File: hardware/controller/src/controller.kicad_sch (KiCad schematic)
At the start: 39 parts, among them J1 To Display, J2 Display, J3 Barrel_Jack_Switch, J4 Program, J5 JTAG, SW1 RESET, SW2 BTN1, SW3 BTN1, U1 ESP32-WROOM-E, U2 XL1509-5.0, U3 XL1509-3.3, U4 RS0102YH8

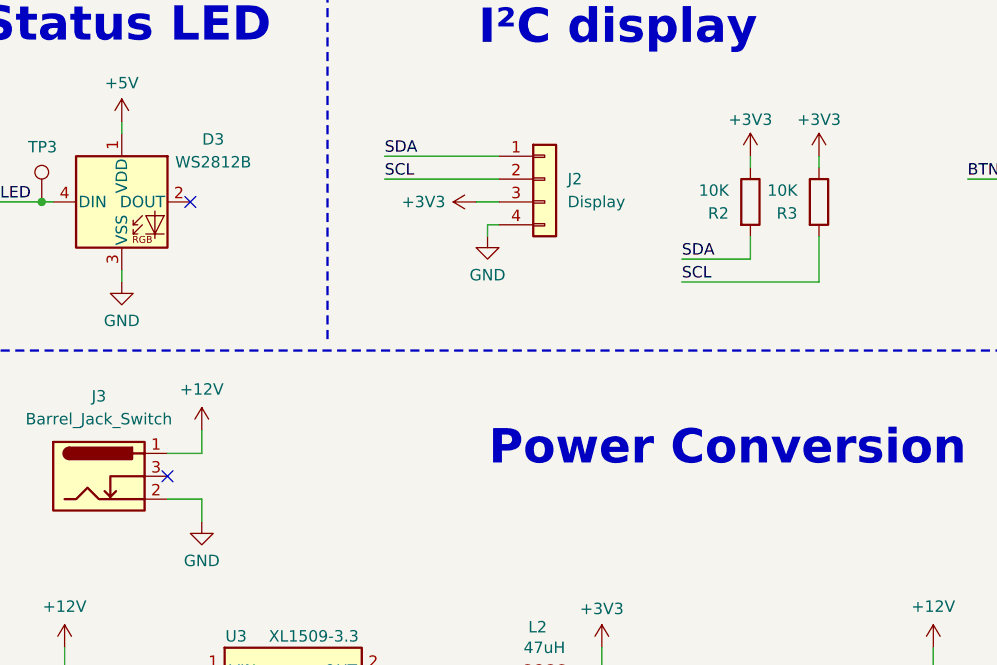
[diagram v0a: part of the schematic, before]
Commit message: connect dc jack ground pin
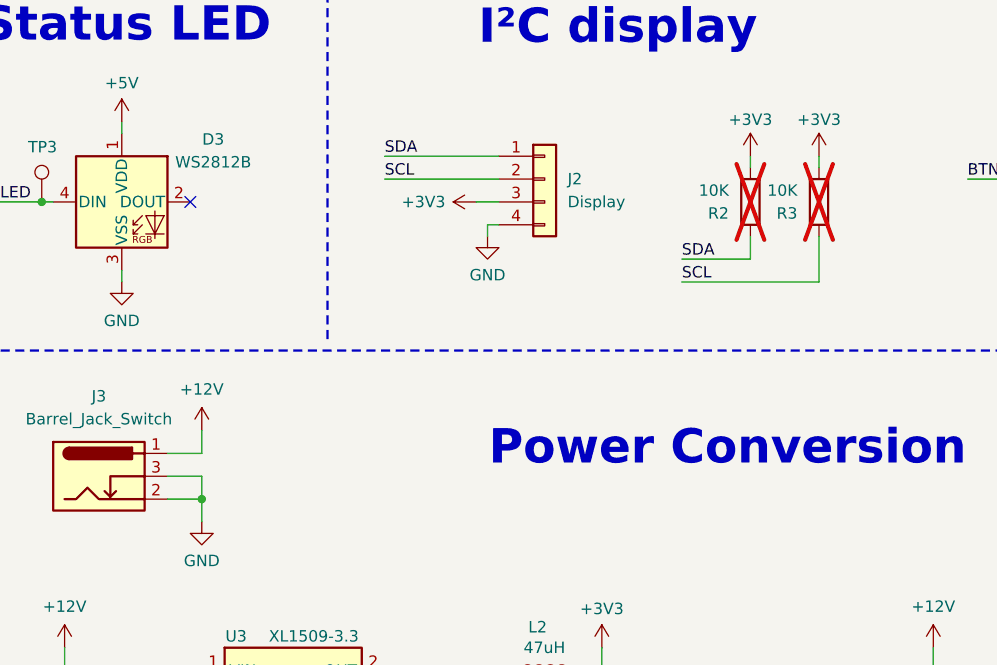
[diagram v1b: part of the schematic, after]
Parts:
- R2, R3: now not fitted; now left out of the parts list
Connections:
- net GND: now also J3.3
- no-connect marks 16 -> 15
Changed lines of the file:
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@@
 		(title "Controller")
 		(date "${DATE}")
-		(rev "2.0.3 DEV")
+		(rev "2.0.4 DEV")
 		(company "OpenFlap")
 		(comment 1 "${GIT_TAG}")
@@
 	)
 	(junction
+		(at 43.18 161.29)
+		(diameter 0)
+		(color 0 0 0 0)
+	)
+	(junction
 		(at 184.15 180.34)
 		(diameter 0)
@@
 	)
 	(no_connect
-		(at 39.37 158.75)
-	)
-	(no_connect
 		(at 100.33 68.58)
 	)
@@
 	(wire
 		(pts
+			(xy 43.18 158.75) (xy 43.18 161.29)
+		)
+		(stroke
+			(width 0)
+			(type default)
+		)
+	)
+	(wire
+		(pts
 			(xy 74.93 180.34) (xy 74.93 181.61)
 		)
@@
 	(wire
 		(pts
+			(xy 39.37 158.75) (xy 43.18 158.75)
+		)
+		(stroke
+			(width 0)
+			(type default)
+		)
+	)
+	(wire
+		(pts
 			(xy 128.27 125.73) (xy 134.62 125.73)
 		)
@@
 		(unit 1)
 		(exclude_from_sim no)
-		(in_bom yes)
+		(in_bom no)
 		(on_board yes)
-		(dnp no)
+		(dnp yes)
 		(property "Reference" "R3"
 			(at 108.204 129.54 0)
@@
 		(unit 1)
 		(exclude_from_sim no)
-		(in_bom yes)
+		(in_bom no)
 		(on_board yes)
-		(dnp no)
+		(dnp yes)
 		(property "Reference" "R2"
 			(at 100.584 129.54 0)

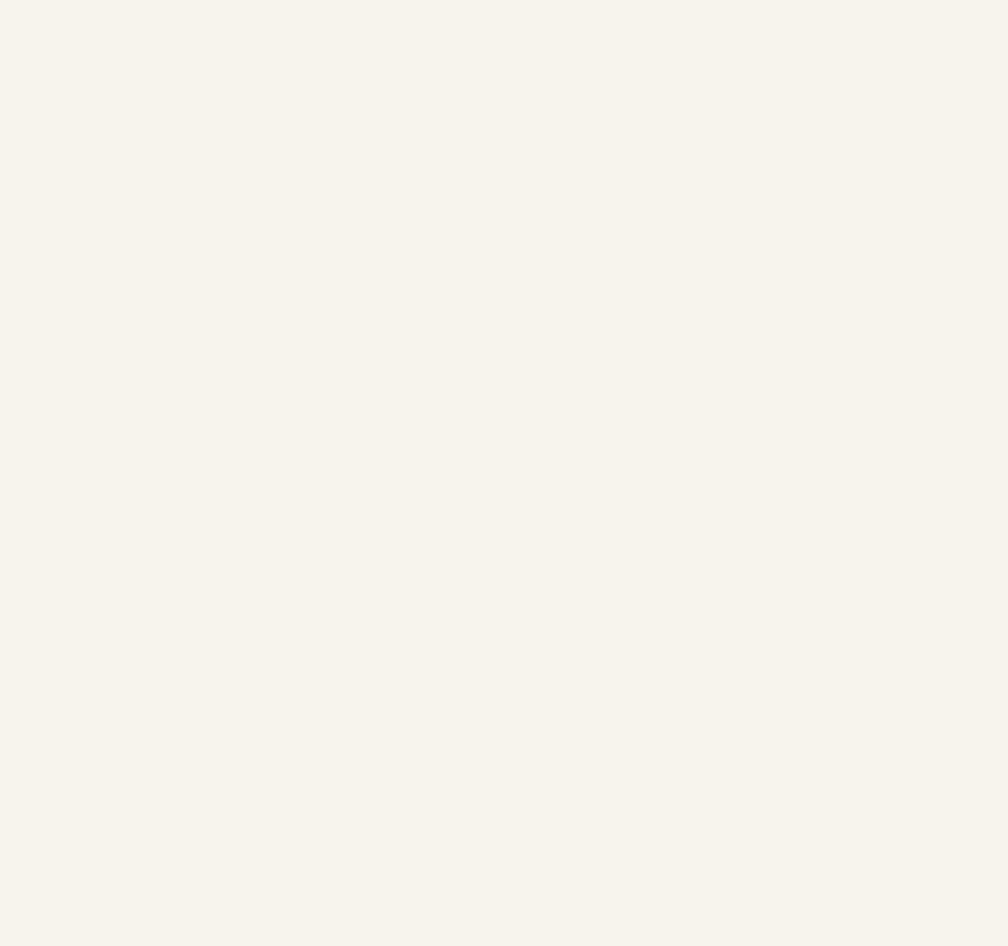
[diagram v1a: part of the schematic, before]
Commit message: Update side panel to add proper ESD protection, 12V detection, removed uart switch in favor of software switching, shuffled around some IO for improved routing.
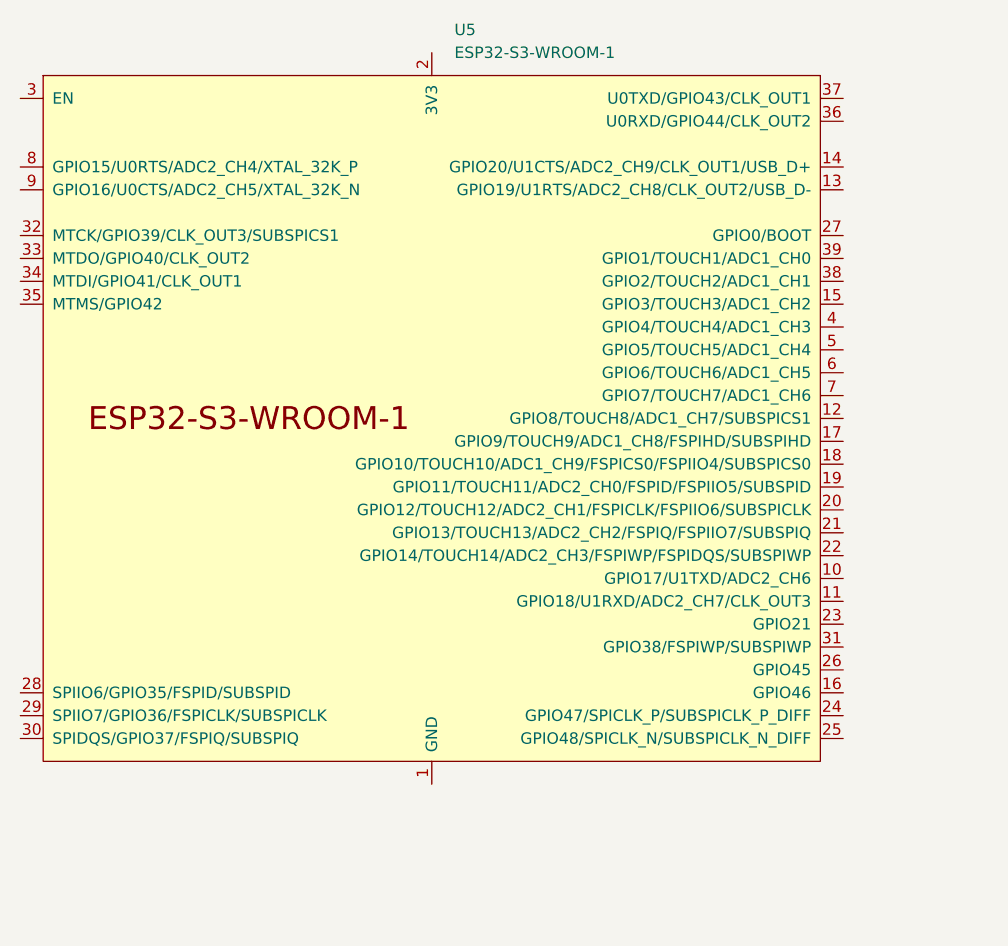
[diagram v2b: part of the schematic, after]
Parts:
- added U5: ESP32-S3-WROOM-1, PCM_Espressif:ESP32-S3-WROOM-1, symbol PCM_Espressif:ESP32-S3-WROOM-1
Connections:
- new net: U5.1 (GND), U5.40 (GND), U5.41 (GND)
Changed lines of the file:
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@@
+	)
+	(symbol
+		(lib_id "PCM_Espressif:ESP32-S3-WROOM-1")
+		(at -91.44 46.99 0)
+		(unit 1)
+		(exclude_from_sim no)
+		(in_bom yes)
+		(on_board yes)
+		(dnp no)
+		(fields_autoplaced yes)
+		(property "Reference" "U5"
+			(at -88.928 3.81 0)
+			(effects
+				(font
+					(size 1.27 1.27)
+				)
+				(justify left)
+			)
+		)
+		(property "Value" "ESP32-S3-WROOM-1"
+			(at -88.928 6.35 0)
+			(effects
+				(font
+					(size 1.27 1.27)
+				)
+				(justify left)
+			)
+		)
+		(property "Footprint" "PCM_Espressif:ESP32-S3-WROOM-1"
+			(at -88.9 95.25 0)
+			(effects
+				(font
+					(size 1.27 1.27)
+				)
+				(hide yes)
+			)
+		)
+		(property "Datasheet" "https://www.espressif.com/sites/default/files/documentation/esp32-s3-wroom-1_wroom-1u_datasheet_en.pdf"
+			(at -88.9 97.79 0)
+			(effects
+				(font
+					(size 1.27 1.27)
+				)
+				(hide yes)
+			)
+		)
+		(property "Description" "2.4 GHz WiFi (802.11 b/g/n) and Bluetooth ® 5 (LE) module Built around ESP32S3 series of SoCs, Xtensa ® dualcore 32bit LX7 microprocessor Flash up to 16 MB, PSRAM up to 8 MB 36 GPIOs, rich set of peripherals Onboard PCB antenna"
+			(at -91.44 46.99 0)
+			(effects
+				(font
+					(size 1.27 1.27)
+				)
+				(hide yes)
+			)
+		)
+		(pin "1"
+		)
+		(pin "7"
+		)
+		(pin "2"
+		)
+		(pin "22"
+		)
+		(pin "21"
+		)
+		(pin "33"
+		)
+		(pin "8"
+		)
+		(pin "15"
+		)
+		(pin "31"
+		)
+		(pin "13"
+		)
+		(pin "19"
+		)
+		(pin "26"
+		)
+		(pin "11"
+		)
+		(pin "14"
+		)
+		(pin "20"
+		)
+		(pin "3"
+		)
+		(pin "39"
+		)
+		(pin "38"
+		)
+		(pin "25"
+		)
+		(pin "16"
+		)
+		(pin "32"
+		)
+		(pin "27"
+		)
+		(pin "30"
+		)
+		(pin "35"
+		)
+		(pin "18"
+		)
+		(pin "37"
+		)
+		(pin "23"
+		)
+		(pin "34"
+		)
+		(pin "4"
+		)
+		(pin "41"
+		)
+		(pin "5"
+		)
+		(pin "6"
+		)
+		(pin "12"
+		)
+		(pin "40"
+		)
+		(pin "10"
+		)
+		(pin "29"
+		)
+		(pin "28"
+		)
+		(pin "17"
+		)
+		(pin "24"
+		)
+		(pin "36"
+		)
+		(pin "9"
+		)
+		(instances
+			(project ""
+				(path "/06f043e8-01fc-418e-a431-ea0e6a8c9987"
+					(reference "U5")
+					(unit 1)
+				)
+			)
+		)
 	)
 	(symbol
